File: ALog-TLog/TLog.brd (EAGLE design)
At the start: 124.1 x 45.3 mm, 94 parts, among them IC1 ATMEGA644M, J6 5.5x2.1mm Barrel, Q1 220mA/50V/3.5Ω, Q5 4.3A/20V/54mΩ, Q6 4.3A/20V/54mΩ, Q7 4.3A/20V/54mΩ, Q8 220mA/50V/3.5Ω, Q9 220mA/50V/3.5Ω, U2 FT231X-Q, U3 915MHz, U4 SX1509

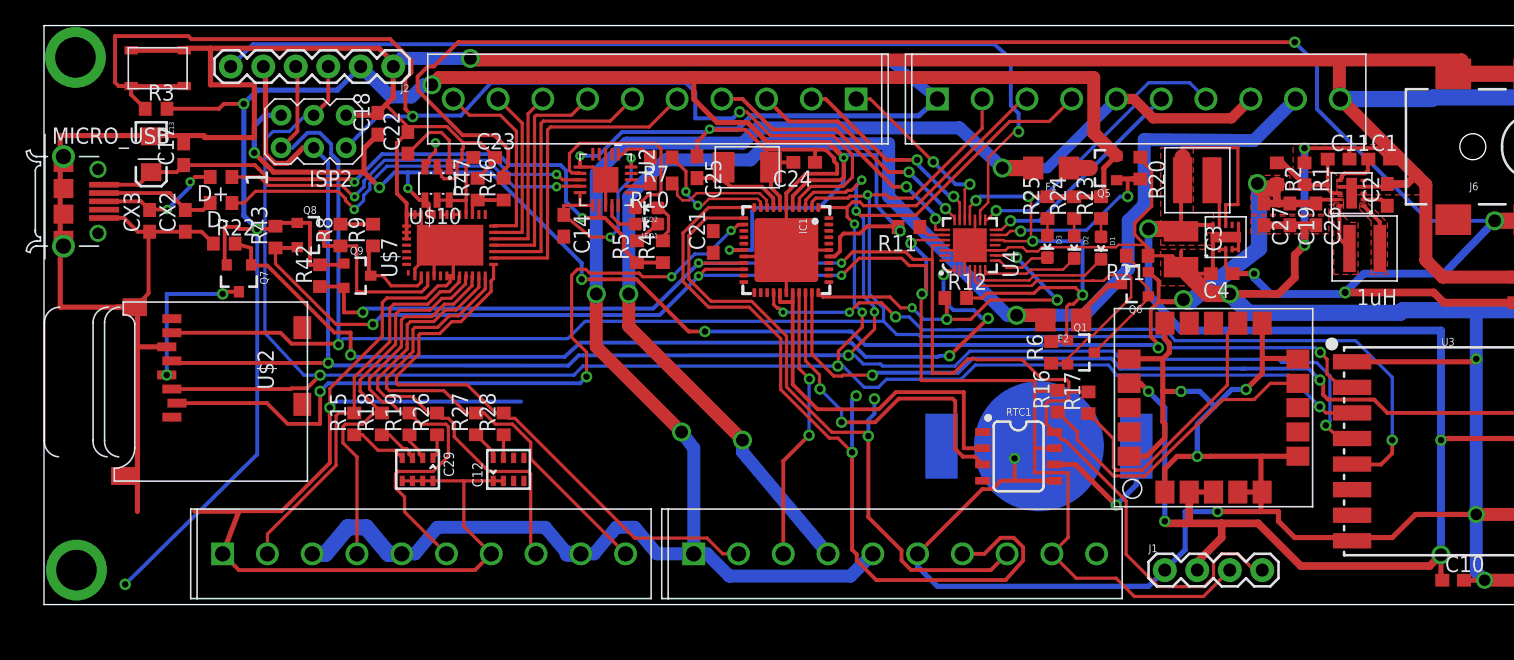
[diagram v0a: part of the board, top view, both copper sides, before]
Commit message: TLog Board Ready for Review
TLog board is at functional stage and ready for review by general eyes, High Speed ADC daughter board preliminary files also added (location may change eventually)
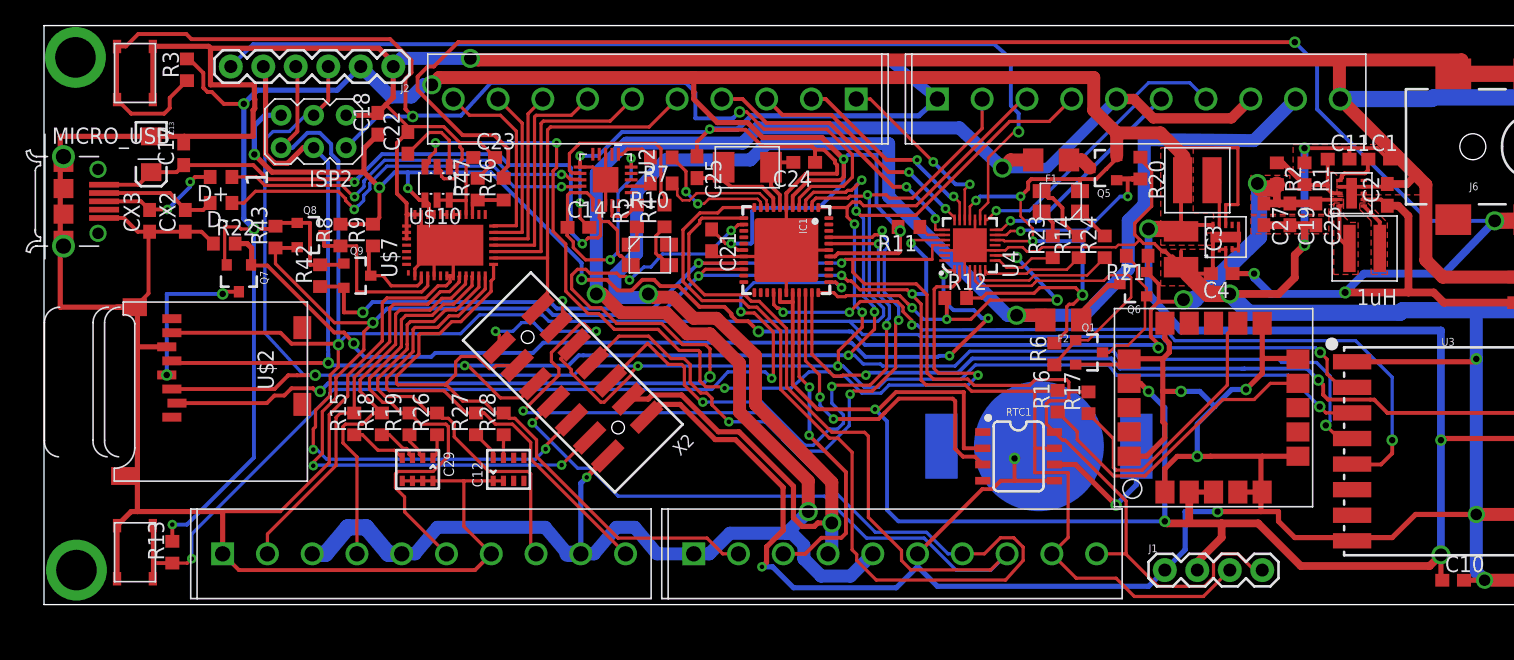
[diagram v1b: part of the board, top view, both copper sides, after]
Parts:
- removed D1, D2, D3: (no value), SparkFun-LED:LED-0603
- removed LED1: Yellow, SparkFun-LED:LED-0603
- removed LED2: Blue, SparkFun-LED:LED-0603
- removed R25: 330, rcl:R0603
- added R13: 10k, resistor:R0603
- added R14: 330, resistor:R0603
- added U$15, U$16: CLVBA-FKA, bschulz:CLVBA-FKA
- added U$5: SKRPABE010, Custom:SKRPABE010_(SWITCH)
- added X2: 87832-14, con-molex:87832-14
- R23, R24: device rcl:R0603 -> resistor:R0603
- R6: value 10k -> (none)
- moved R23 4.86 mm to (79.0, 28.1)
- moved R3 3.89 mm to (11.3, 41.9), turned to 90 degrees
- moved R24 3.88 mm to (83.1, 28.1)
- moved R4 2.80 mm to (48.6, 30.5)
- moved R5 2.79 mm to (46.5, 30.5)
- moved U$9 1.82 mm to (7.24, 41.7), turned to 270 degrees
- moved C14 1.15 mm to (41.9, 29.6), turned to 0 degrees
- moved F1 0.63 mm to (78.9, 34.9)
- moved Q1 0.63 mm to (81.8, 19.8)
- moved R6 0.28 mm to (79.1, 19.7)
- moved C21 0.18 mm to (52.3, 28.6), turned to 270 degrees
- moved Q6 0.13 mm to (85.3, 25.1)
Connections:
- removed net 3.3V: C10.1, C21.1, C3.1, IC1.17, IC1.27, IC1.29, IC1.38, IC1.5, J1.2, J2.2, L2.P$2, Q1.1, Q5.2, Q7.2, Q8.1, Q9.1, R11.2, R12.2, R23.2, R24.2, R25.2, R3.2, R42.2, R43.2, R6.2, RTC1.2, U$4.P$10, U$4.P$8, U$6.17, U$6.2, U$6.3, U3.13, U4.12, U4.18, U4.4
- removed net N$32: D1.A, R23.1
- removed net N$33: D2.A, R24.1
- removed net N$34: D3.A, R25.1
- removed net N$40: LED2.A, R4.2
- removed net N$42: LED1.A, R5.2
- new net 3V3: C10.1, C21.1, C3.1, IC1.17, IC1.27, IC1.29, IC1.38, IC1.5, J1.2, J2.2, L2.P$2, Q5.2, Q7.2, Q8.1, Q9.1, R11.2, R12.2, R13.2, R3.2, R42.2, R43.2, R6.2, RTC1.2, U$15.2, U$4.P$10, U$4.P$8, U$6.17, U$6.2, U$6.3, U3.13, U4.12, U4.18, U4.4
- new net D1_UNIV: IC1.40, X2.5
- new net D2_UNIV: IC1.41, X2.14
- new net LOG_INT: IC1.34, R13.1, U$5.P$3, U$5.P$4
- new net N$10: R23.2, U$15.4
- new net N$15: R24.2, U$15.1
- new net N$16: R5.1, U$16.1
- new net N$26: R4.1, U$16.3
- new net N$9: R14.2, U$15.3
- net 5V: now also R21.1
- net 5V_EXT_CTRL: now also Q1.1; no longer Q1.2
- net ADC5: now also X2.12
- net ADC6: now also X2.13
- net EXT_3.3V: now also X2.2
- net EXT_5V: now also X2.3
- net GND: now also Q1.2, U$5.P$1, U$5.P$2, X2.1; no longer R21.1
- net LED1: now also R24.1; no longer D1.C
- net LED2: now also R14.1; no longer D2.C
- net LED3: now also R23.1; no longer D3.C
- net MISO: now also X2.6
- net MOSI: now also X2.9
- net N$41: now also R4.2; no longer LED2.C
- net N$43: now also R5.2; no longer LED1.C
- net RX_EXT: now also X2.7
- net SCK: now also X2.10
- net SCL: now also X2.11
- net SDA: now also X2.4
- net TX_EXT: now also X2.8
- net VUSB: now also U$16.2; no longer R4.1, R5.1
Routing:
- net 3V3: track 0.00 -> 432.5 mm, vias 0 -> 17
- net 3.3V: track 401.4 -> 0.00 mm, vias 16 -> 0
- net LOG_INT: track 0.00 -> 78.0 mm, vias 0 -> 4
- net REF_CTRL: track 2.22 -> 75.2 mm, vias 1 -> 4
- net D2_UNIV: track 0.00 -> 70.9 mm, vias 0 -> 6
- net D1_UNIV: track 0.00 -> 46.6 mm, vias 0 -> 4
- net GND: track 795.4 -> 840.7 mm, vias 15 -> 16
- net TX_EXT: track 52.7 -> 94.9 mm, vias 2 -> 1
- net RX_EXT: track 65.4 -> 99.3 mm, vias 2 -> 1
- net MISO: track 153.3 -> 187.1 mm, vias 3 -> 5
- net SDA: track 123.9 -> 156.5 mm, vias 5 -> 7
- net EXT_5V: track 110.8 -> 137.9 mm
- net EXT_3.3V: track 143.9 -> 160.6 mm, vias 3 -> 4
- net SD_CS: track 59.7 -> 74.5 mm
- net MOSI: track 159.8 -> 169.8 mm, vias 5 -> 6
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- added copper zone on layer 1, net 3V3
- removed copper zone on layer 1, net 3.3V

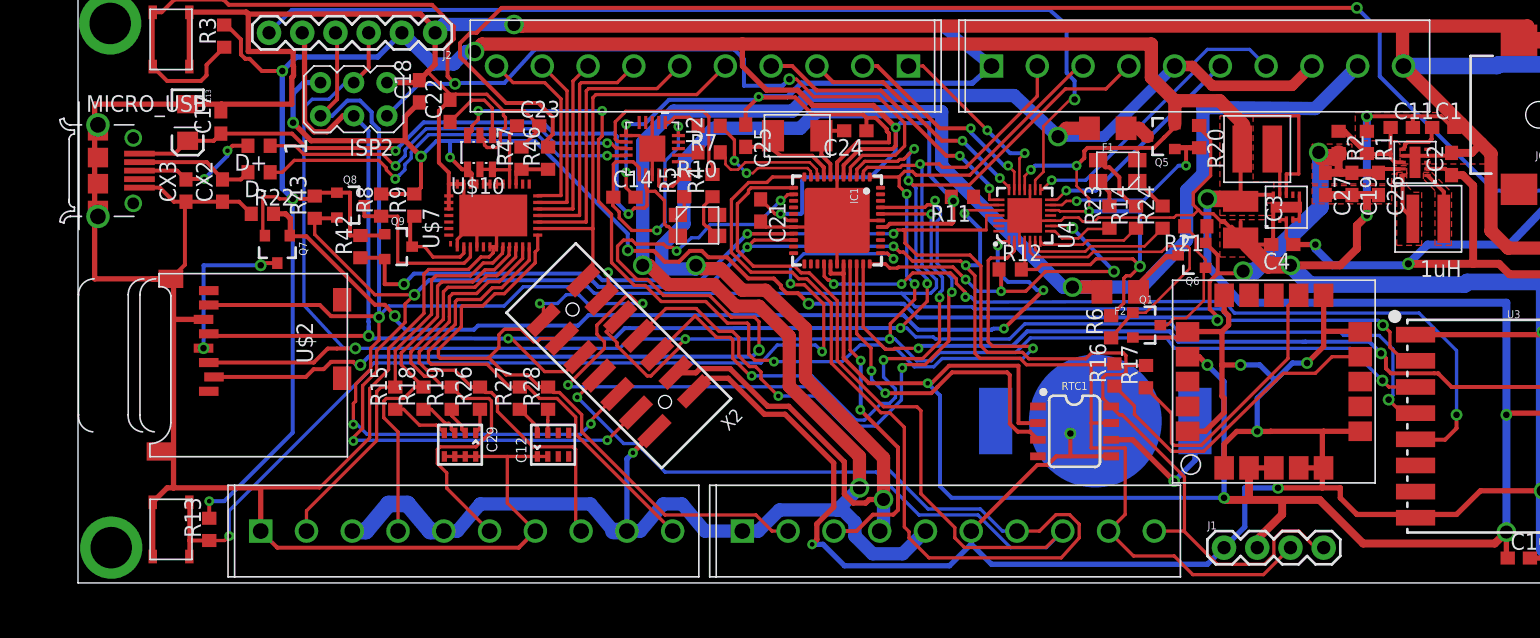
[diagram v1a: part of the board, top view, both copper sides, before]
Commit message: In Progress of modifying board for auto BOM
Working on cleaning up the board and libraries such that an auto BOM can be formed, also beginning to clean up silk screen for first run of PCBs
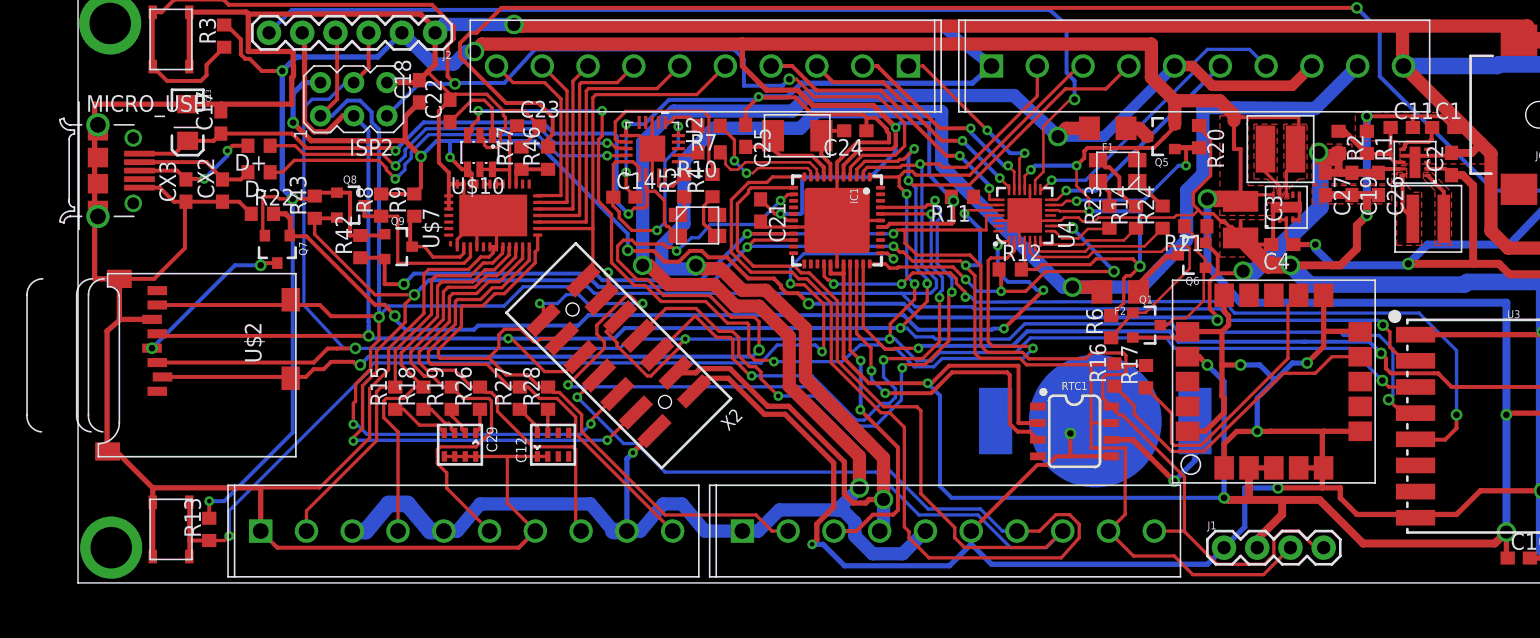
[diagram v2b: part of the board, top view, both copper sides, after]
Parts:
- IC1: device atmel:MLF44-TH -> bschulz:MLF44-TH
- J10, J5, J8, J9: device SparkFun-Connectors:SCREWTERMINAL-3.5MM-10 -> bschulz:1X10_3.5MM_SCREW
- L2: device Custom:WE-LQS(INDUCTOR) -> bschulz:WE-LQS(4X4)
- Q5, Q6, Q7: value 4.3A/20V/54mΩ -> MOSFET_PCH-IRLML2244; device SparkFun-DiscreteSemi:SOT23-3 -> bschulz:SOT23-3
- Q8, Q9: value 220mA/50V/3.5Ω -> MOSFET-NCH-BSS138; device SparkFun-DiscreteSemi:SOT23-3 -> bschulz:SOT23-3
- RTC1: device SparkFun-Clocks:SO08 -> bschulz:SO08
- U$10: value MAX6070 -> MAX6070AAUT18
- U$2: device adafruit:MICROSD -> bschulz:MICROSD
- U$3: device Custom:WSON-10 -> bschulz:WSON-10
- U$4: value TPS6217X -> TPS6217XTPS62177; device texas:WSON-10 -> bschulz:WSON-10
- U$5, U$9: device Custom:SKRPABE010_(SWITCH) -> bschulz:SKRPABE010_(SWITCH)
- U$7: device linear-technology:QFN38-5X7 -> bschulz:QFN38-5X7
- U$8: device Custom:WE-MAIA(4.1X4.1) -> bschulz:WE-MAIA(4.1X4.1)
- U4: device SparkFun-IC-Special-Function:QFN-28 -> bschulz:QFN-28
- moved U$2 3.94 mm to (16.8, 23.7)
- moved L2 1.78 mm to (92.1, 33.3), turned to 0 degrees
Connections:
- net N$5: now also U$1.OSC2; no longer U$1.P$2
- net N$8: now also U$1.OSC1; no longer U$1.P$1
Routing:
- net MISO: track 187.1 -> 191.1 mm
- net SD_CS: track 74.5 -> 78.5 mm
- net MOSI: track 169.8 -> 173.8 mm
- net SCK: track 177.5 -> 181.3 mm
- added copper zone on layer 1, net N$2

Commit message: Fixed silk screen and capacitor size
Fixed the silk screen layout and changed capacitor sizes on the buck-boost converter (From all 0603 to some 0805 and some 1206)
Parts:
- C19, C26, C27: device rcl:C0603 -> rcl:C1206
- C2: device rcl:C0603 -> rcl:C0805
- C3: device rcl:C1210 -> rcl:C1206
- MICRO_USB: value 10118194-0001LF_LONGER_PADS -> MICRO_USB_LONGPADS; device 10118194-0001LF:10118194-0001LF_LONGER_PADS -> bschulz:10118194-0001LF_10118194-0001LF_LONGER_PADS
- moved R2 1.27 mm to (95.5, 34.5)
- moved R1 0.76 mm to (98.7, 34.5)
- moved U$8 0.51 mm to (103.4, 27.4)
- moved C19 0.38 mm to (97.5, 30.2)
- moved C26 0.38 mm to (99.6, 30.2)
- moved C27 0.38 mm to (95.5, 30.2)
- moved L2 0.25 mm to (91.8, 33.3)
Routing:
- net 5V: track 129.5 -> 131.3 mm
- net GND: track 840.5 -> 842.2 mm
- net N$6: track 8.08 -> 9.08 mm
- net N$3: track 3.84 -> 4.34 mm
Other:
- board text added: "RST"
- board text removed: "RESET"

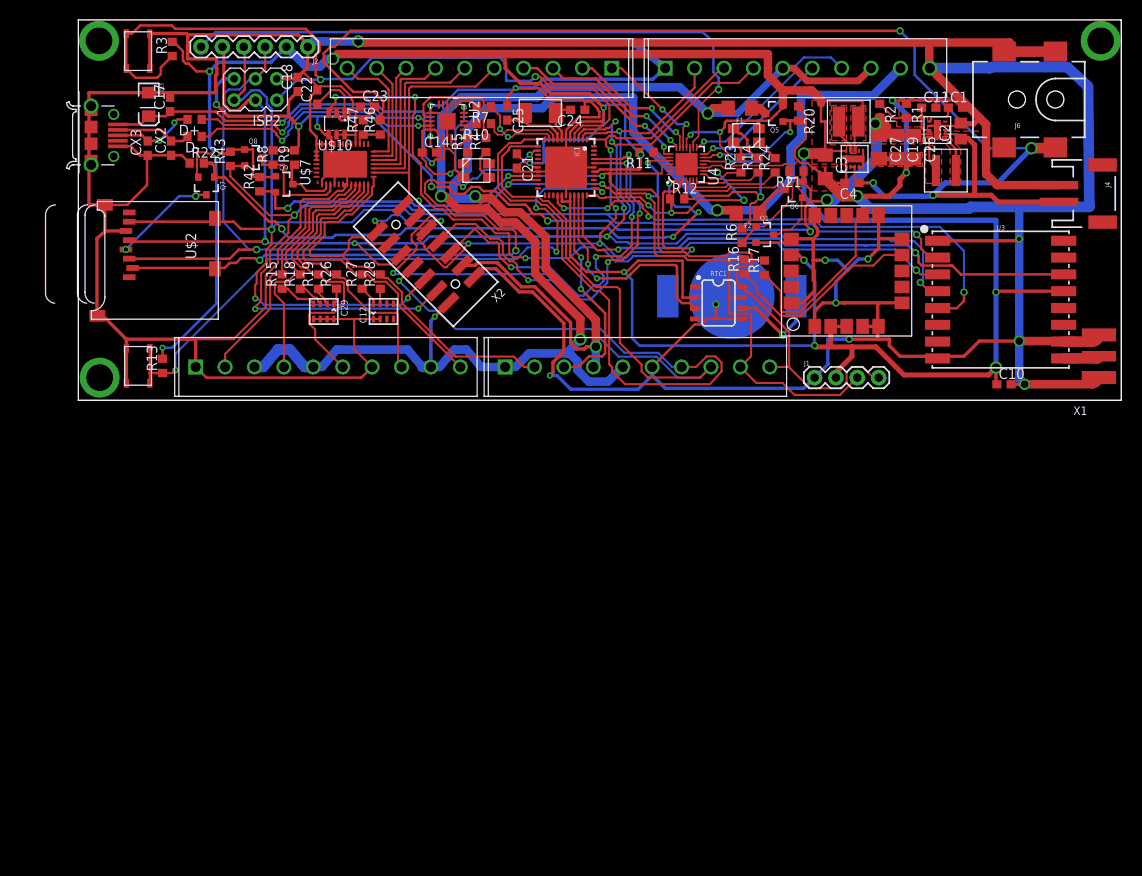
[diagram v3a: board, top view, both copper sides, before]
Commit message: updated 5V regulator footprint, trace fixes
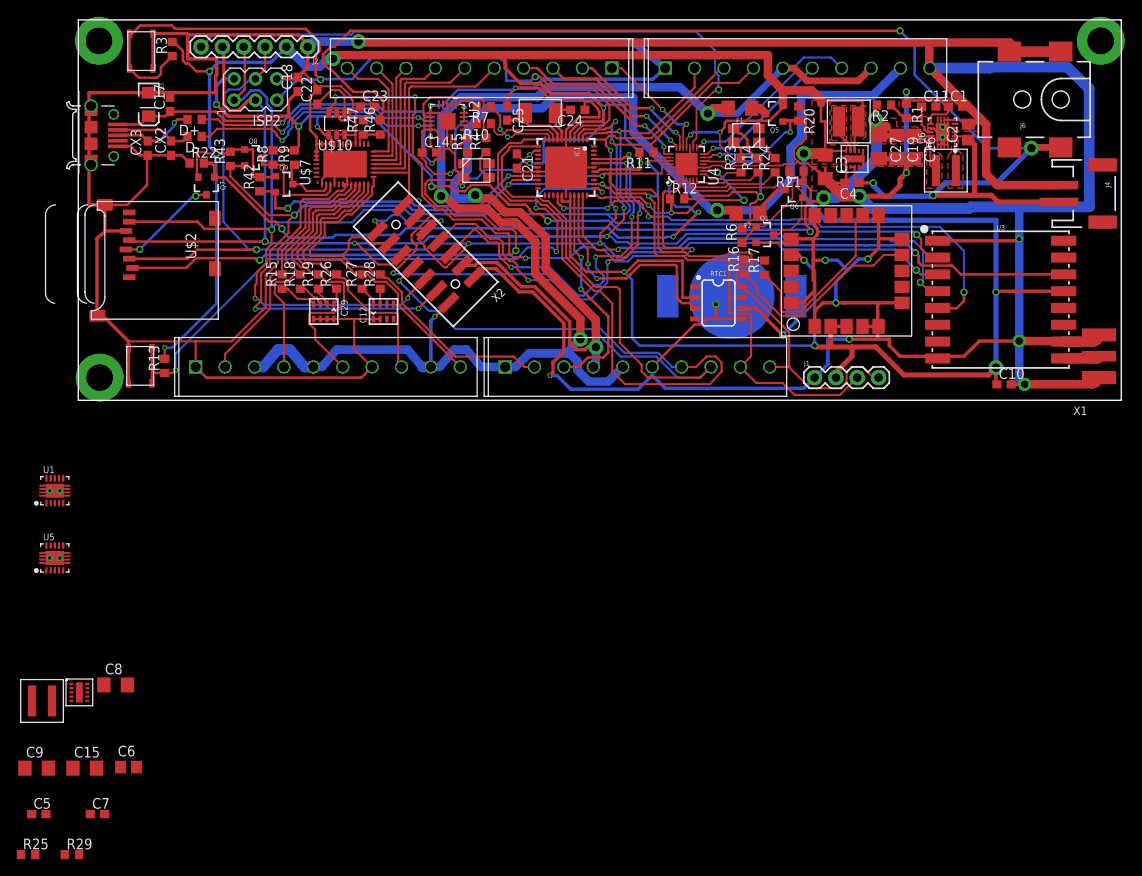
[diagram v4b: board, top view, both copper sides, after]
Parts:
- removed U$3: TPS63061, bschulz:WSON-10
- added C15, C8, C9: 22uF, rcl:C1206
- added C5: 0.1uF, rcl:C0603
- added C6: 10uF, rcl:C0805
- added C7: 10pF, rcl:C0603
- added R25: 143k, rcl:R0603
- added R29: 953k, rcl:R0603
- added U$13: TPS63061, bschulz:WSON-10
- added U$17: 1uH, bschulz:WE-MAIA(4.1X4.1)
- added U1, U5, U6: (no value), microbuilder:PWSON-N10
- moved C2 0.90 mm to (106.0, 32.0)
- moved R2 0.86 mm to (96.0, 35.2), turned to 180 degrees
- moved J6 0.63 mm to (117.0, 35.9)
- moved U$9 0.38 mm to (7.62, 41.7)
- moved U$5 0.25 mm to (7.49, 4.19)
- moved R13 0.25 mm to (10.4, 4.19)
- moved C1 0.13 mm to (104.5, 35.1)
- moved C11 0.13 mm to (101.3, 35.1)
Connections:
- removed net N$1: U$3.P$10, U$8.P$2
- removed net N$3: U$3.P$1, U$8.P$1
- new net N$29: U5.10
- new net N$32: U$8.P$1, U6.1
- new net N$33: U$13.P$10, U$17.P$2
- new net N$34: U$13.P$1, U$17.P$1
- new net N$40: C5.1, U$13.P$6
- new net N$42: C7.1, R25.2, R29.1, U$13.P$8
- new net N$47: U$8.P$2, U6.10
- new net PGND: U1.THERMAL@1, U1.THERMAL@10, U1.THERMAL@11, U1.THERMAL@12, U1.THERMAL@13, U1.THERMAL@14, U1.THERMAL@5, U1.THERMAL@6, U1.THERMAL@7, U1.THERMAL@8, U1.THERMAL@9, U5.THERMAL@1, U5.THERMAL@10, U5.THERMAL@11, U5.THERMAL@12, U5.THERMAL@13, U5.THERMAL@14, U5.THERMAL@5, U5.THERMAL@6, U5.THERMAL@7, U5.THERMAL@8, U5.THERMAL@9
- new net VIN: U1.2, U5.2
- new net VOUT: U1.9, U5.9
- net 5V: now also C15.1, C8.1, C9.1, R29.2, U$13.P$9, U6.9; no longer U$3.P$9
- net BATT+: now also C6.1, U$13.P$2, U$13.P$3, U6.2, U6.3; no longer U$3.P$2, U$3.P$3
- net GND: now also C15.2, C5.2, C6.2, C7.2, C8.2, C9.2, R25.1, U$13.P$11, U$13.P$4, U$13.P$7, U1.7, U5.7, U6.4, U6.7, U6.THERMAL@1, U6.THERMAL@10, U6.THERMAL@11, U6.THERMAL@12, U6.THERMAL@13, U6.THERMAL@14, U6.THERMAL@5, U6.THERMAL@6, U6.THERMAL@7, U6.THERMAL@8, U6.THERMAL@9; no longer U$3.P$11, U$3.P$4, U$3.P$7
- net N$4: now also U6.6; no longer U$3.P$6
- net N$6: now also U6.8; no longer U$3.P$8
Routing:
- net N$3: track 4.34 -> 0.00 mm
- net N$1: track 4.04 -> 0.00 mm
- net N$47: track 0.00 -> 3.85 mm
- net N$32: track 0.00 -> 3.61 mm
- net 3V3: track 432.7 -> 434.7 mm
- net N$6: track 9.08 -> 7.97 mm
- net RST: track 93.9 -> 93.1 mm
- added copper zone on layer 1, net N$32
- added copper zone on layer 1, net N$47
- removed copper zone on layer 1, net N$1
- removed copper zone on layer 1, net N$3
